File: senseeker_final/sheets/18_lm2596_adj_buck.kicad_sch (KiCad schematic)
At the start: 15 parts, among them J20 Conn_01x01_Pin, J21 Conn_01x01_Pin, J22 Conn_01x01_Pin, J23 Conn_01x01_Pin, U30 LM2596S-ADJ

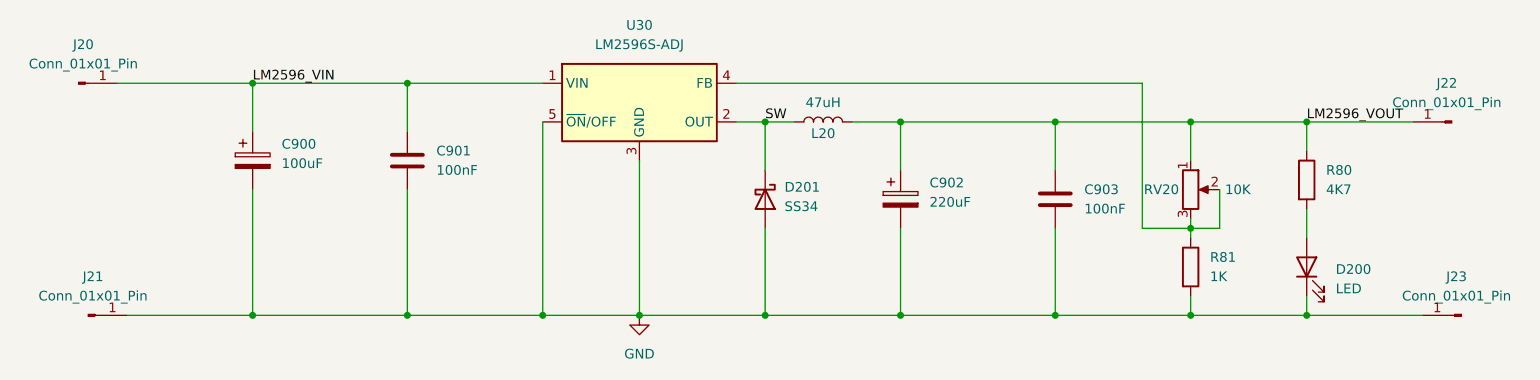
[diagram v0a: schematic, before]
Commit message: formatting changes for LM2596, now ready to branch of off and make our seperate PCB and then compare
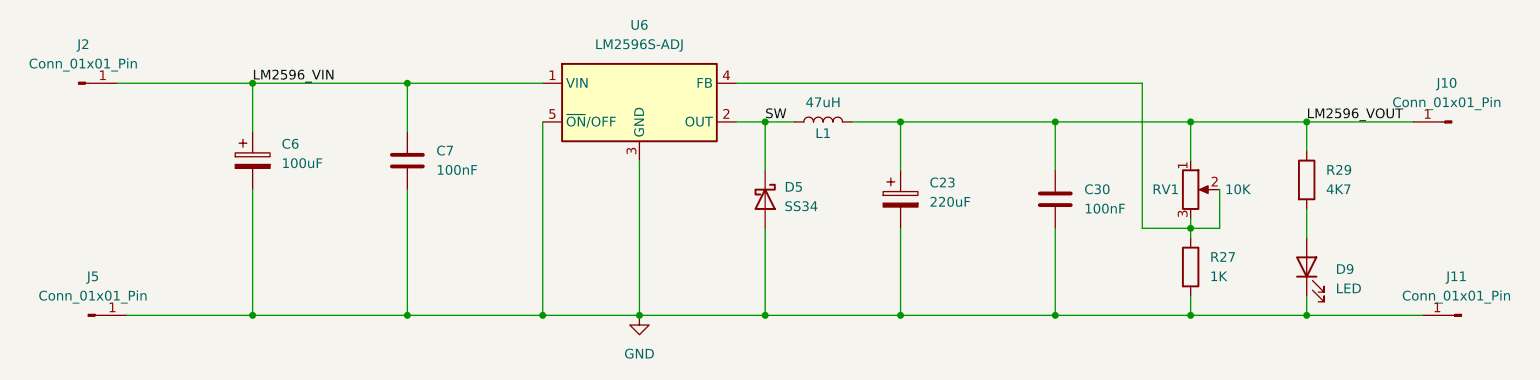
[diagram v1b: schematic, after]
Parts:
- renumbered C902 to C23, C903 to C30, C900 to C6, C901 to C7, D201 to D5, D200 to D9, J22 to J10, J23 to J11, J20 to J2, J21 to J5, L20 to L1, R81 to R27, R80 to R29, RV20 to RV1, U30 to U6
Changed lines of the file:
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@@
 		(on_board yes)
 		(dnp no)
-		(property "Reference" "L20"
+		(property "Reference" "L1"
 			(at 156.21 95.504 90)
 			(effects
@@
 			(project "senseeker_final"
 				(path "/529bc8a5-ffae-43ac-972d-caccc3afab85/9dddee0f-db6b-4d06-95d5-93553e494b2c"
-					(reference "L20")
+					(reference "L1")
 					(unit 1)
 				)
@@
 		(dnp no)
 		(fields_autoplaced yes)
-		(property "Reference" "D201"
+		(property "Reference" "D5"
 			(at 151.13 102.5524 90)
 			(effects
@@
 			(project "senseeker_final"
 				(path "/529bc8a5-ffae-43ac-972d-caccc3afab85/9dddee0f-db6b-4d06-95d5-93553e494b2c"
-					(reference "D201")
+					(reference "D5")
 					(unit 1)
 				)
@@
 		(dnp no)
 		(fields_autoplaced yes)
-		(property "Reference" "C901"
+		(property "Reference" "C7"
 			(at 105.41 97.7899 0)
 			(effects
@@
 			(project "senseeker_final"
 				(path "/529bc8a5-ffae-43ac-972d-caccc3afab85/9dddee0f-db6b-4d06-95d5-93553e494b2c"
-					(reference "C901")
+					(reference "C7")
 					(unit 1)
 				)
@@
 		(dnp no)
 		(fields_autoplaced yes)
-		(property "Reference" "J23"
+		(property "Reference" "J11"
 			(at 239.395 114.3 0)
 			(effects
@@
 			(project "senseeker_final"
 				(path "/529bc8a5-ffae-43ac-972d-caccc3afab85/9dddee0f-db6b-4d06-95d5-93553e494b2c"
-					(reference "J23")
+					(reference "J11")
 					(unit 1)
 				)
@@
 		(dnp no)
 		(fields_autoplaced yes)
-		(property "Reference" "#PWR01"
+		(property "Reference" "#PWR02"
 			(at 132.08 125.73 0)
 			(effects
@@
 			(project "senseeker_final"
 				(path "/529bc8a5-ffae-43ac-972d-caccc3afab85/9dddee0f-db6b-4d06-95d5-93553e494b2c"
-					(reference "#PWR01")
+					(reference "#PWR02")
 					(unit 1)
 				)
@@
 		(dnp no)
 		(fields_autoplaced yes)
-		(property "Reference" "C902"
+		(property "Reference" "C23"
 			(at 170.18 101.9809 0)
 			(effects
@@
 			(project "senseeker_final"
 				(path "/529bc8a5-ffae-43ac-972d-caccc3afab85/9dddee0f-db6b-4d06-95d5-93553e494b2c"
-					(reference "C902")
+					(reference "C23")
 					(unit 1)
 				)
@@
 		(dnp no)
 		(fields_autoplaced yes)
-		(property "Reference" "J20"
+		(property "Reference" "J2"
 			(at 59.055 83.82 0)
 			(effects
@@
 			(project "senseeker_final"
 				(path "/529bc8a5-ffae-43ac-972d-caccc3afab85/9dddee0f-db6b-4d06-95d5-93553e494b2c"
-					(reference "J20")
+					(reference "J2")
 					(unit 1)
 				)
@@
 		(on_board yes)
 		(dnp no)
-		(property "Reference" "RV20"
+		(property "Reference" "RV1"
 			(at 202.946 102.87 0)
 			(effects
@@
 			(project "senseeker_final"
 				(path "/529bc8a5-ffae-43ac-972d-caccc3afab85/9dddee0f-db6b-4d06-95d5-93553e494b2c"
-					(reference "RV20")
+					(reference "RV1")
 					(unit 1)
 				)
@@
 		(dnp no)
 		(fields_autoplaced yes)
-		(property "Reference" "D200"
+		(property "Reference" "D9"
 			(at 223.52 113.3474 90)
 			(effects
@@
 			(project "senseeker_final"
 				(path "/529bc8a5-ffae-43ac-972d-caccc3afab85/9dddee0f-db6b-4d06-95d5-93553e494b2c"
-					(reference "D200")
+					(reference "D9")
 					(unit 1)
 				)
@@
 		(dnp no)
 		(fields_autoplaced yes)
-		(property "Reference" "R80"
+		(property "Reference" "R29"
 			(at 222.25 100.3299 0)
 			(effects
@@
 			(project "senseeker_final"
 				(path "/529bc8a5-ffae-43ac-972d-caccc3afab85/9dddee0f-db6b-4d06-95d5-93553e494b2c"
-					(reference "R80")
+					(reference "R29")
 					(unit 1)
 				)
@@
 		(dnp no)
 		(fields_autoplaced yes)
-		(property "Reference" "R81"
+		(property "Reference" "R27"
 			(at 207.01 111.7599 0)
 			(effects
@@
 			(project "senseeker_final"
 				(path "/529bc8a5-ffae-43ac-972d-caccc3afab85/9dddee0f-db6b-4d06-95d5-93553e494b2c"
-					(reference "R81")
+					(reference "R27")
 					(unit 1)
 				)
@@
 		(dnp no)
 		(fields_autoplaced yes)
-		(property "Reference" "U30"
+		(property "Reference" "U6"
 			(at 132.08 81.28 0)
 			(effects
@@
 			(project "senseeker_final"
 				(path "/529bc8a5-ffae-43ac-972d-caccc3afab85/9dddee0f-db6b-4d06-95d5-93553e494b2c"
-					(reference "U30")
+					(reference "U6")
 					(unit 1)
 				)
@@
 		(dnp no)
 		(fields_autoplaced yes)
-		(property "Reference" "J22"
+		(property "Reference" "J10"
 			(at 238.125 88.9 0)
 			(effects
@@
 			(project "senseeker_final"
 				(path "/529bc8a5-ffae-43ac-972d-caccc3afab85/9dddee0f-db6b-4d06-95d5-93553e494b2c"
-					(reference "J22")
+					(reference "J10")
 					(unit 1)
 				)
@@
 		(dnp no)
 		(fields_autoplaced yes)
-		(property "Reference" "C903"
+		(property "Reference" "C30"
 			(at 190.5 102.8699 0)
 			(effects
@@
 			(project "senseeker_final"
 				(path "/529bc8a5-ffae-43ac-972d-caccc3afab85/9dddee0f-db6b-4d06-95d5-93553e494b2c"
-					(reference "C903")
+					(reference "C30")
 					(unit 1)
 				)
@@
 		(dnp no)
 		(fields_autoplaced yes)
-		(property "Reference" "C900"
+		(property "Reference" "C6"
 			(at 85.09 96.9009 0)
 			(effects
@@
 			(project "senseeker_final"
 				(path "/529bc8a5-ffae-43ac-972d-caccc3afab85/9dddee0f-db6b-4d06-95d5-93553e494b2c"
-					(reference "C900")
+					(reference "C6")
 					(unit 1)
 				)
@@
 		(dnp no)
 		(fields_autoplaced yes)
-		(property "Reference" "J21"
+		(property "Reference" "J5"
 			(at 60.325 114.3 0)
 			(effects
@@
 			(project "senseeker_final"
 				(path "/529bc8a5-ffae-43ac-972d-caccc3afab85/9dddee0f-db6b-4d06-95d5-93553e494b2c"
-					(reference "J21")
-					(unit 1)
-				)
+					(reference "J5")
+					(unit 1)
+				)
